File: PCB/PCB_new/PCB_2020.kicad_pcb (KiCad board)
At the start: 2 copper layers, 102.2 x 94.5 mm, 26 parts, among them IC1 LM358N, J1 TI_CONN, Q1 220mA/50V/3.5Ω, Q2 100V/17A, Q3 100V/17A, Q4 100V/17A, Q5 100V/17A, Q6 100V/17A

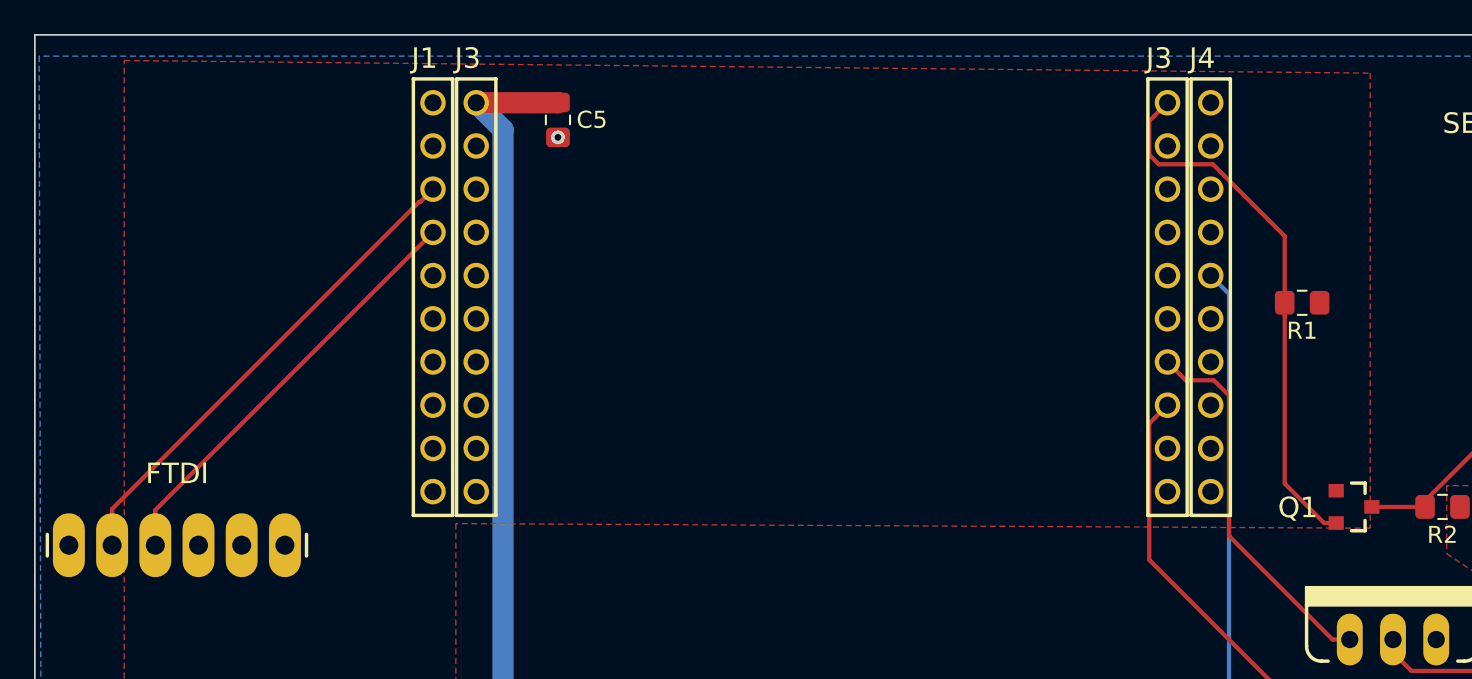
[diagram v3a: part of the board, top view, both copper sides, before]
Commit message: added ftdi 3d model and cleaned up .pretty folder
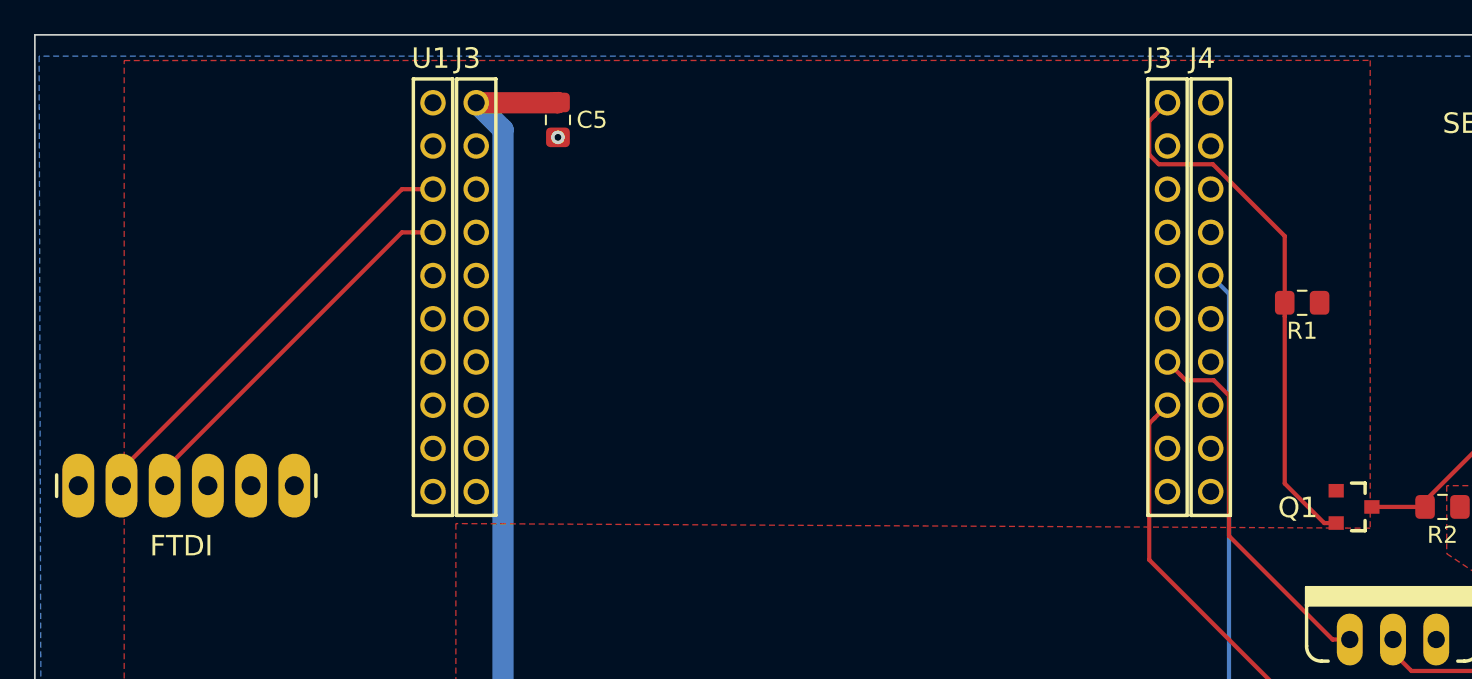
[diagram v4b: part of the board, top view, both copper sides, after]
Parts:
- CONN1: footprint Drivetrain_control:1X06_LONGPADS -> Drivetrain_control:FTDI_CONN
- moved CONN1 3.54 mm to (98.3, 73.2)
- renumbered J1 to U1
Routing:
- net SCIB_RX: track 28.8 -> 26.1 mm
- net SCIB_TX: track 25.2 -> 22.5 mm
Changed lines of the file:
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@@
     (thickness 1.6)
     (drawings 1)
-    (tracks 135)
+    (tracks 136)
     (zones 0)
     (modules 26)
@@
   (page A4)
   (layers
-    (0 Top signal hide)
-    (31 Bottom signal hide)
+    (0 Top signal)
+    (31 Bottom signal)
     (32 B.Adhes user)
     (33 F.Adhes user)
@@
     (add_net +5V)
   )
+  (module Drivetrain_control:FTDI_CONN (layer Top)
+    (at 98.3 73.25)
+    (descr "ftdi (usb) to uart converter")
+    (fp_text reference CONN1 (at -1.27 -2.032 -180) (layer F.Fab)
+      (effects (font (size 1.2065 1.2065) (thickness 0.2413)) (justify left bottom))
+    )
+    (fp_text value FTDI (at 4.2 4.25 -180) (layer F.SilkS)
+      (effects (font (size 1.2065 1.2065) (thickness 0.2413)) (justify left bottom))
+    )
+    (fp_poly (pts (xy -0.254 0.254) (xy 0.254 0.254) (xy 0.254 -0.254) (xy -0.254 -0.254)) (layer F.Fab) (width 0))
+    (fp_poly (pts (xy 2.286 0.254) (xy 2.794 0.254) (xy 2.794 -0.254) (xy 2.286 -0.254)) (layer F.Fab) (width 0))
+    (fp_poly (pts (xy 4.826 0.254) (xy 5.334 0.254) (xy 5.334 -0.254) (xy 4.826 -0.254)) (layer F.Fab) (width 0))
+    (fp_poly (pts (xy 7.366 0.254) (xy 7.874 0.254) (xy 7.874 -0.254) (xy 7.366 -0.254)) (layer F.Fab) (width 0))
+    (fp_poly (pts (xy 9.906 0.254) (xy 10.414 0.254) (xy 10.414 -0.254) (xy 9.906 -0.254)) (layer F.Fab) (width 0))
+    (fp_poly (pts (xy 12.446 0.254) (xy 12.954 0.254) (xy 12.954 -0.254) (xy 12.446 -0.254)) (layer F.Fab) (width 0))
+    (fp_line (start 13.97 -0.635) (end 13.97 0.635) (layer F.SilkS) (width 0.2032))
+    (fp_line (start -1.27 -0.635) (end -1.27 0.635) (layer F.SilkS) (width 0.2032))
+    (pad 6 thru_hole oval (at 12.7 0 90) (size 3.7592 1.8796) (drill 1.1176) (layers *.Cu *.Mask)
+      (net 3 GND) (solder_mask_margin 0.0762))
+    (pad 5 thru_hole oval (at 10.16 0 90) (size 3.7592 1.8796) (drill 1.1176) (layers *.Cu *.Mask)
+      (solder_mask_margin 0.0762))
+    (pad 4 thru_hole oval (at 7.62 0 90) (size 3.7592 1.8796) (drill 1.1176) (layers *.Cu *.Mask)
+      (net 1 +3V3) (solder_mask_margin 0.0762))
+    (pad 3 thru_hole oval (at 5.08 0 90) (size 3.7592 1.8796) (drill 1.1176) (layers *.Cu *.Mask)
+      (net 10 SCIB_TX) (solder_mask_margin 0.0762))
+    (pad 2 thru_hole oval (at 2.54 0 90) (size 3.7592 1.8796) (drill 1.1176) (layers *.Cu *.Mask)
+      (net 9 SCIB_RX) (solder_mask_margin 0.0762))
+    (pad 1 thru_hole oval (at 0 0 90) (size 3.7592 1.8796) (drill 1.1176) (layers *.Cu *.Mask)
+      (solder_mask_margin 0.0762))
+    (model ${KISYS3DMOD}/Connector_PinHeader_2.54mm.3dshapes/PinHeader_1x06_P2.54mm_Vertical.step
+      (at (xyz 0 0 0))
+      (scale (xyz 1 1 1))
+      (rotate (xyz 0 0 -90))
+    )
+    (model "${MITCHS_CAD}/ft231x-breakout-v11 v2.step"
+      (offset (xyz -1.25 26.6 3))
+      (scale (xyz 1 1 1))
+      (rotate (xyz 0 0 90))
+    )
+  )
   (module Resistor_SMD:R_0805_2012Metric_Pad1.15x1.40mm_HandSolder (layer Top)
     (at 183.5 82.25 180)
@@
     )
   )
-  (module Drivetrain_control:1X06_LONGPADS (layer Top)
-    (at 97.75 76.75)
-    (descr "<h3>Plated Through Hole - 6 Pin with Long Pads</h3>\n<p>Specifications:\n<ul><li>Pin count:6</li>\n<li>Pin pitch:0.1\"</li>\n</ul></p>\n<p>Example device(s):\n<ul><li>CONN_06</li>\n</ul></p>")
-    (fp_text reference CONN1 (at 3.25 4.5 180) (layer F.Fab)
-      (effects (font (size 1.2065 1.2065) (thickness 0.2413)) (justify left bottom))
-    )
-    (fp_text value FTDI (at 4.5 -3.5 180) (layer F.SilkS)
-      (effects (font (size 1.2065 1.2065) (thickness 0.2413)) (justify left bottom))
-    )
-    (fp_poly (pts (xy -0.254 0.254) (xy 0.254 0.254) (xy 0.254 -0.254) (xy -0.254 -0.254)) (layer F.Fab) (width 0))
-    (fp_poly (pts (xy 2.286 0.254) (xy 2.794 0.254) (xy 2.794 -0.254) (xy 2.286 -0.254)) (layer F.Fab) (width 0))
-    (fp_poly (pts (xy 4.826 0.254) (xy 5.334 0.254) (xy 5.334 -0.254) (xy 4.826 -0.254)) (layer F.Fab) (width 0))
-    (fp_poly (pts (xy 7.366 0.254) (xy 7.874 0.254) (xy 7.874 -0.254) (xy 7.366 -0.254)) (layer F.Fab) (width 0))
-    (fp_poly (pts (xy 9.906 0.254) (xy 10.414 0.254) (xy 10.414 -0.254) (xy 9.906 -0.254)) (layer F.Fab) (width 0))
-    (fp_poly (pts (xy 12.446 0.254) (xy 12.954 0.254) (xy 12.954 -0.254) (xy 12.446 -0.254)) (layer F.Fab) (width 0))
-    (fp_line (start 13.97 -0.635) (end 13.97 0.635) (layer F.SilkS) (width 0.2032))
-    (fp_line (start -1.27 -0.635) (end -1.27 0.635) (layer F.SilkS) (width 0.2032))
-    (pad 6 thru_hole oval (at 12.7 0 90) (size 3.7592 1.8796) (drill 1.1176) (layers *.Cu *.Mask)
-      (net 3 GND) (solder_mask_margin 0.0762))
-    (pad 5 thru_hole oval (at 10.16 0 90) (size 3.7592 1.8796) (drill 1.1176) (layers *.Cu *.Mask)
-      (solder_mask_margin 0.0762))
-    (pad 4 thru_hole oval (at 7.62 0 90) (size 3.7592 1.8796) (drill 1.1176) (layers *.Cu *.Mask)
-      (net 1 +3V3) (solder_mask_margin 0.0762))
-    (pad 3 thru_hole oval (at 5.08 0 90) (size 3.7592 1.8796) (drill 1.1176) (layers *.Cu *.Mask)
-      (net 10 SCIB_TX) (solder_mask_margin 0.0762))
-    (pad 2 thru_hole oval (at 2.54 0 90) (size 3.7592 1.8796) (drill 1.1176) (layers *.Cu *.Mask)
-      (net 9 SCIB_RX) (solder_mask_margin 0.0762))
-    (pad 1 thru_hole oval (at 0 0 90) (size 3.7592 1.8796) (drill 1.1176) (layers *.Cu *.Mask)
-      (solder_mask_margin 0.0762))
-  )
   (module Drivetrain_control:TI_Footprint (layer Top)
     (at 118 75)
     (descr "<b>THROUGH-HOLE .025\" SQ POST SOCKET</b><p>\nSource: Samtec SSW.pdf")
-    (fp_text reference J1 (at -0.115 -26.164 180) (layer F.SilkS)
+    (fp_text reference U1 (at -0.115 -26.164 180) (layer F.SilkS)
       (effects (font (size 1.2065 1.2065) (thickness 0.09652)) (justify left bottom))
     )
@@
   (segment (start 169.225 58.579998) (end 165.001003 54.356001) (width 0.25) (layer Top) (net 8))
   (segment (start 169.225 62.5) (end 169.225 58.579998) (width 0.25) (layer Top) (net 8))
-  (segment (start 100.29 74.6204) (end 100.29 76.75) (width 0.25) (layer Top) (net 9))
-  (segment (start 118.339401 56.570999) (end 100.29 74.6204) (width 0.25) (layer Top) (net 9))
-  (segment (start 118.405001 56.570999) (end 118.339401 56.570999) (width 0.25) (layer Top) (net 9))
-  (segment (start 119.155 55.821) (end 118.405001 56.570999) (width 0.25) (layer Top) (net 9))
-  (segment (start 102.83 74.686) (end 102.83 76.75) (width 0.25) (layer Top) (net 10))
-  (segment (start 119.155 58.361) (end 102.83 74.686) (width 0.25) (layer Top) (net 10))
+  (segment (start 100.84 72.3102) (end 100.84 73.25) (width 0.25) (layer Top) (net 9))
+  (segment (start 117.3292 55.821) (end 100.84 72.3102) (width 0.25) (layer Top) (net 9))
+  (segment (start 119.155 55.821) (end 117.3292 55.821) (width 0.25) (layer Top) (net 9))
+  (segment (start 118.09434 58.361) (end 119.155 58.361) (width 0.25) (layer Top) (net 10))
+  (segment (start 117.3292 58.361) (end 118.09434 58.361) (width 0.25) (layer Top) (net 10))
+  (segment (start 103.38 72.3102) (end 117.3292 58.361) (width 0.25) (layer Top) (net 10))
+  (segment (start 103.38 73.25) (end 103.38 72.3102) (width 0.25) (layer Top) (net 10))
   (segment (start 163.085199 66.730999) (end 162.3352 65.981) (width 0.25) (layer Top) (net 11))
   (segment (start 163.410201 67.056001) (end 163.085199 66.730999) (width 0.25) (layer Top) (net 11))
@@
     (polygon
       (pts
-        (xy 174.25 49) (xy 174.25 75.75) (xy 120.5 75.480487) (xy 120.5 120.019514) (xy 98.25 120.265642)
+        (xy 174.25 48.25) (xy 174.25 75.75) (xy 120.5 75.480487) (xy 120.5 120.019514) (xy 98.25 120.265642)
         (xy 98.25 112.25) (xy 101 112.241156) (xy 101 48.258845)
       )

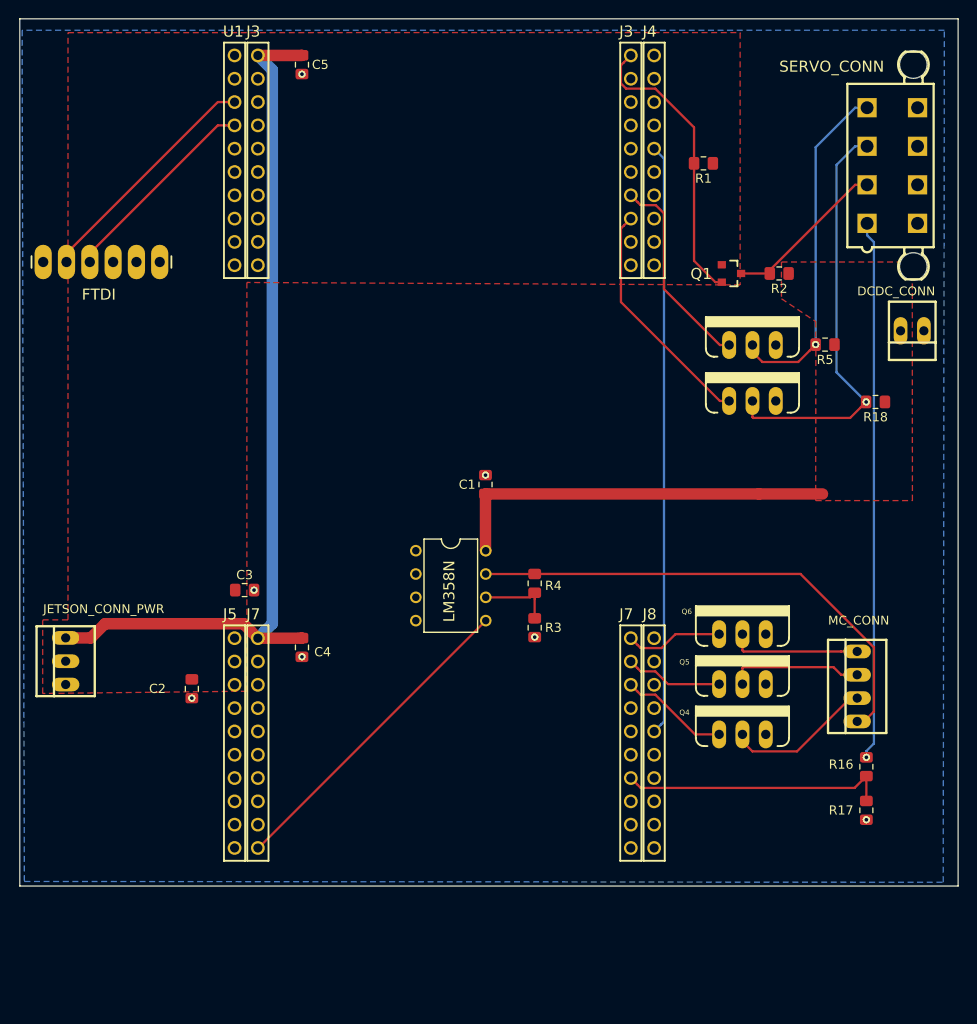
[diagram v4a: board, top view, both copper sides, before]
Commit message: updated footprints to kicad std lib and removed associated custom footprints
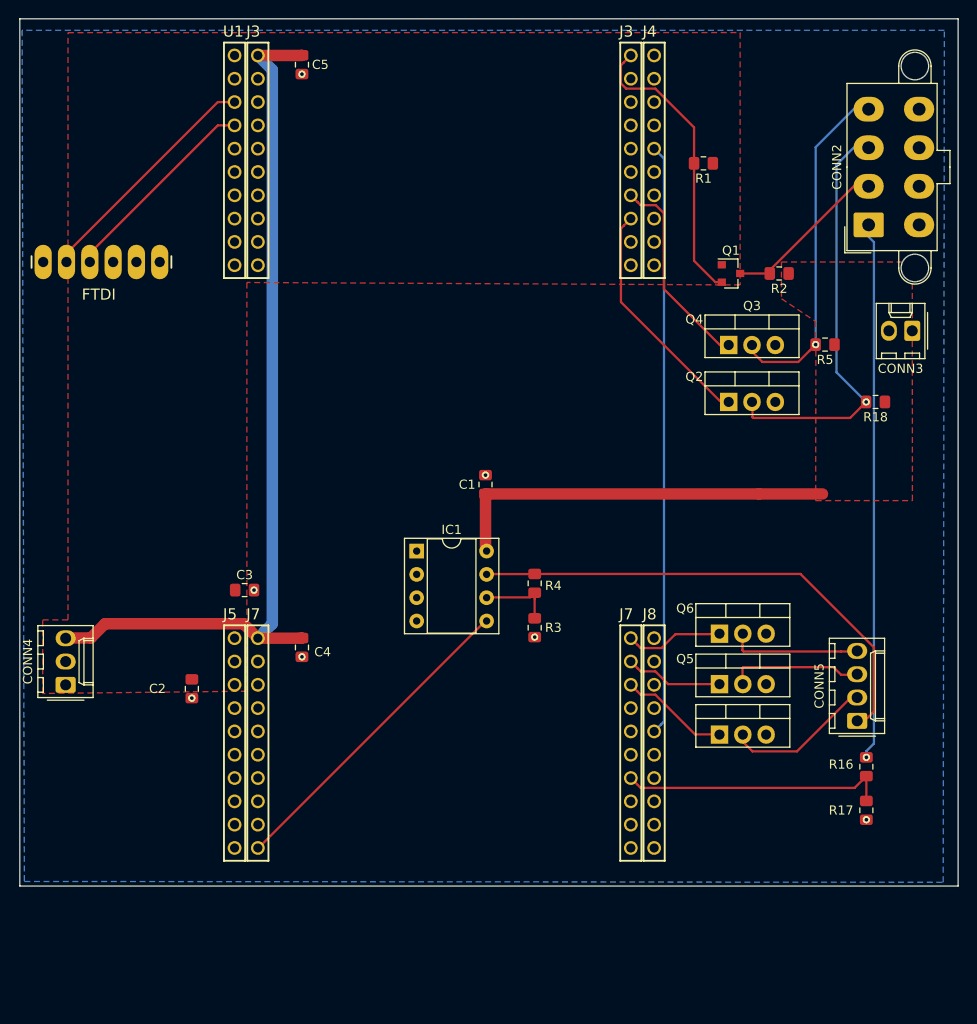
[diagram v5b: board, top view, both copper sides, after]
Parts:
- CONN2: footprint Drivetrain_control:5566-8 -> Connector_Molex:Molex_Mini-Fit_Jr_5566-08A2_2x04_P4.20mm_Vertical
- CONN3: footprint Drivetrain_control:22-23-2021 -> Connector_Molex:Molex_KK-254_AE-6410-02A_1x02_P2.54mm_Vertical
- CONN4: footprint Drivetrain_control:22-23-2031 -> Connector_Molex:Molex_KK-254_AE-6410-03A_1x03_P2.54mm_Vertical
- CONN5: footprint Drivetrain_control:22-23-2041 -> Connector_Molex:Molex_KK-254_AE-6410-04A_1x04_P2.54mm_Vertical
- IC1: footprint Drivetrain_control:DIL08 -> Package_DIP:DIP-8_W7.62mm_Socket
- Q1: footprint Drivetrain_control:SOT23-3 -> Package_TO_SOT_SMD:SOT-23
- Q2, Q3, Q4, Q5, Q6: footprint Drivetrain_control:TO220V -> Package_TO_SOT_THT:TO-220-3_Vertical
- moved CONN2 6.96 mm to (188.2, 69.2), turned to 90 degrees
- moved IC1 5.29 mm to (139.0, 104.8), turned to 0 degrees
- moved CONN5 3.75 mm to (187.0, 123.2)
- moved Q2 2.59 mm to (173.0, 88.5)
- moved Q3 2.59 mm to (173.0, 82.3)
- moved CONN4 2.58 mm to (100.8, 119.3)
- moved Q6 2.50 mm to (172.0, 113.8)
- moved Q4 2.50 mm to (172.0, 124.8)
- moved Q5 2.50 mm to (172.0, 119.2)
- turned Q1 to 0 degrees

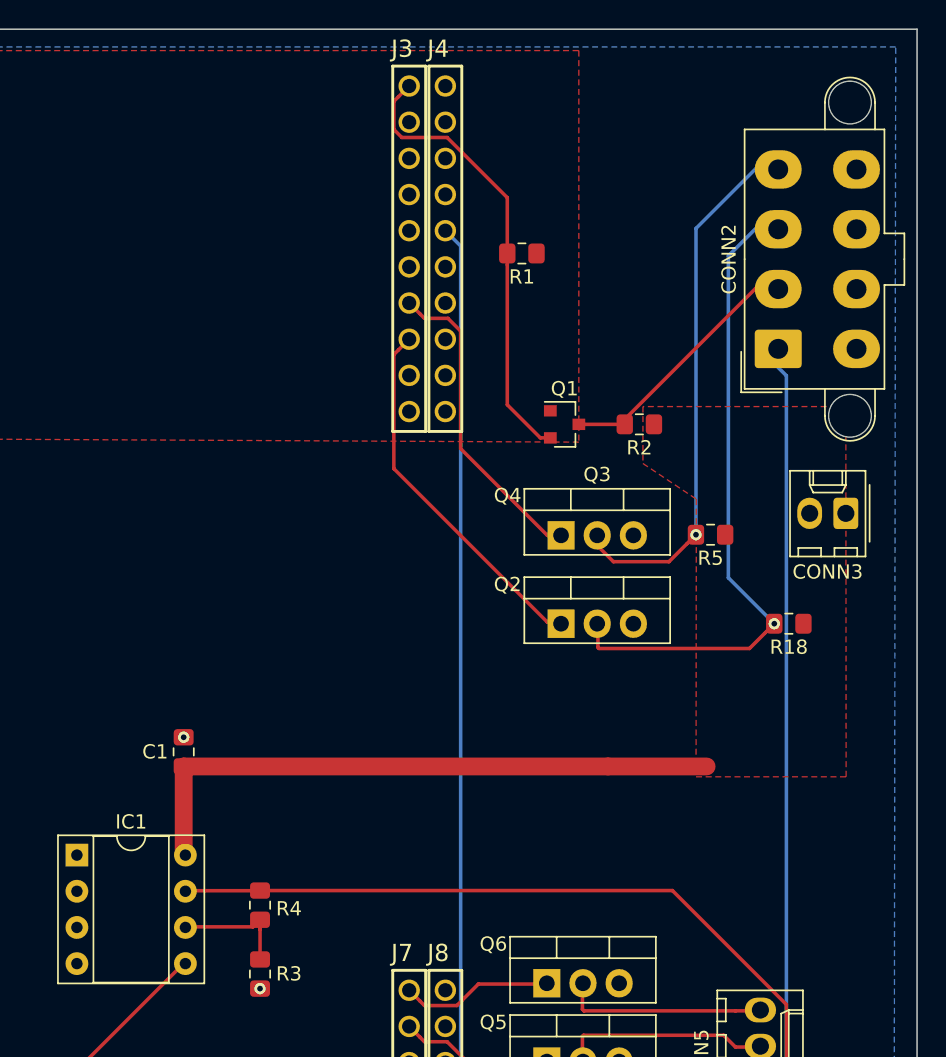
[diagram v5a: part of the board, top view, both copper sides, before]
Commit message: added ti 3d model to footprint
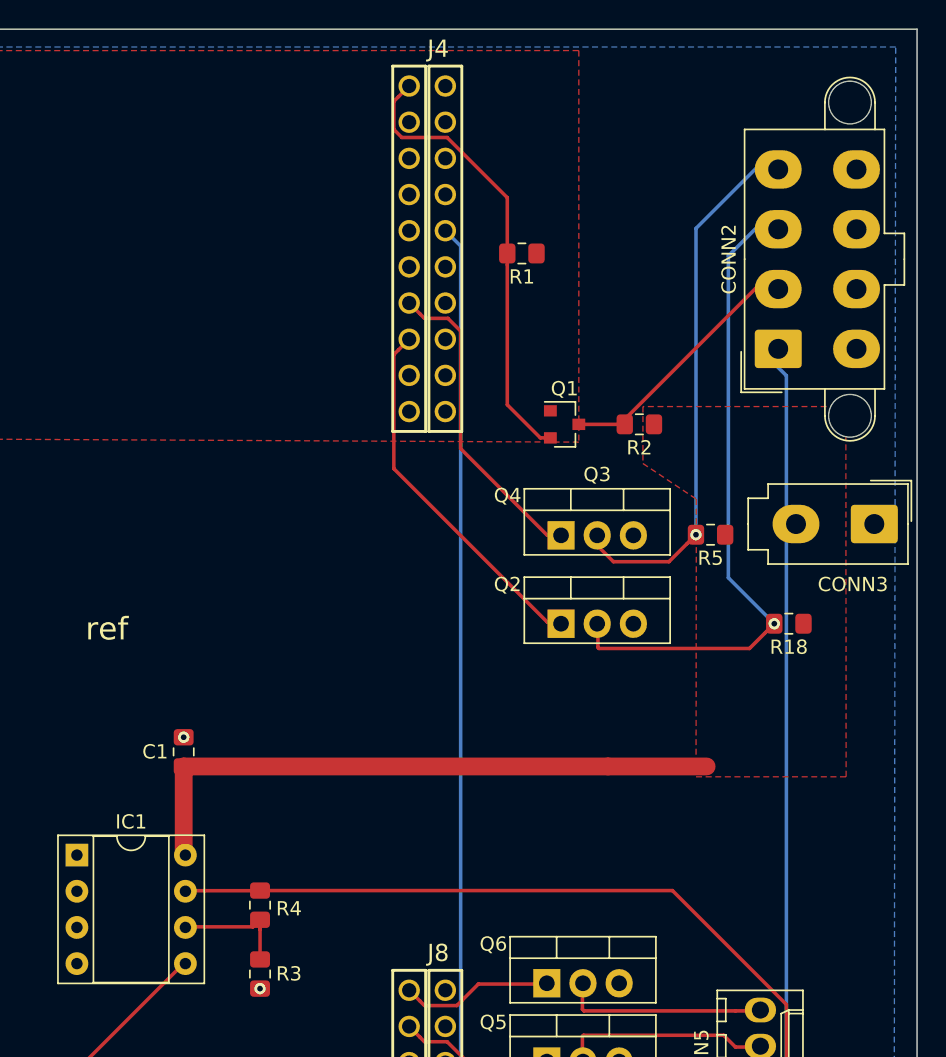
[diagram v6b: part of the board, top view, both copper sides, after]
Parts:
- CONN3: footprint Connector_Molex:Molex_KK-254_AE-6410-02A_1x02_P2.54mm_Vertical -> Connector_Molex:Molex_Mini-Fit_Jr_5566-02A_2x01_P4.20mm_Vertical
- moved CONN3 2.14 mm to (195.0, 81.5), turned to 270 degrees
